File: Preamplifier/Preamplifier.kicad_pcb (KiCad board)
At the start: 2 copper layers, 0 parts

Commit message: Preamplifier Board
Added a preamplifier channel to the board.
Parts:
- added C1: 100n, Capacitor_SMD:C_0805_2012Metric_Pad1.18x1.45mm_HandSolder, F.Cu at (161.0, 84.0)
- added C10: 100n, Capacitor_SMD:C_0805_2012Metric_Pad1.18x1.45mm_HandSolder, F.Cu at (165.3, 144.2)
- added C11: 22n, Capacitor_SMD:C_0805_2012Metric_Pad1.18x1.45mm_HandSolder, F.Cu at (157.5, 94.5)
- added C12: 22n, Capacitor_SMD:C_0805_2012Metric_Pad1.18x1.45mm_HandSolder, F.Cu at (165.3, 147.2)
- added C13: 100n, Capacitor_SMD:C_0805_2012Metric_Pad1.18x1.45mm_HandSolder, F.Cu at (131.9, 137.9)
- added C14: 100n, Capacitor_SMD:C_0805_2012Metric_Pad1.18x1.45mm_HandSolder, F.Cu at (131.9, 140.9)
- added C15: 1u, Capacitor_SMD:C_0805_2012Metric_Pad1.18x1.45mm_HandSolder, F.Cu at (153.5, 91.0)
- added C16: 1u, Capacitor_SMD:C_0805_2012Metric_Pad1.18x1.45mm_HandSolder, F.Cu at (165.3, 150.3)
- added C17: 1u, Capacitor_SMD:C_0805_2012Metric_Pad1.18x1.45mm_HandSolder, F.Cu at (141.0, 88.0)
- added C18: 1u, Capacitor_SMD:C_0805_2012Metric_Pad1.18x1.45mm_HandSolder, F.Cu at (131.9, 143.9)
- added C19: 1u, Capacitor_SMD:C_0805_2012Metric_Pad1.18x1.45mm_HandSolder, F.Cu at (127.5, 85.5)
- added C2: 100n, Capacitor_SMD:C_0805_2012Metric_Pad1.18x1.45mm_HandSolder, F.Cu at (170.0, 84.0)
- added C20: 1u, Capacitor_SMD:C_0805_2012Metric_Pad1.18x1.45mm_HandSolder, F.Cu at (131.9, 146.9)
- added C21: 22u, Capacitor_SMD:CP_Elec_6.3x5.8, F.Cu at (116.5, 83.2)
- added C22: 22u, Capacitor_SMD:CP_Elec_6.3x5.8, F.Cu at (139.6, 140.5)
- added C23: 100n, Capacitor_SMD:C_0805_2012Metric_Pad1.18x1.45mm_HandSolder, F.Cu at (180.7, 79.0)
- added C24: 100n, Capacitor_SMD:C_0805_2012Metric_Pad1.18x1.45mm_HandSolder, F.Cu at (131.9, 149.9)
- added C25: 1u, Capacitor_SMD:C_0805_2012Metric_Pad1.18x1.45mm_HandSolder, F.Cu at (180.7, 83.0)
- added C26: 1u, Capacitor_SMD:C_0805_2012Metric_Pad1.18x1.45mm_HandSolder, F.Cu at (131.9, 153.0)
- added C3: 100p, Capacitor_SMD:C_0805_2012Metric_Pad1.18x1.45mm_HandSolder, F.Cu at (172.5, 91.0)
- added C4: 100p, Capacitor_SMD:C_0805_2012Metric_Pad1.18x1.45mm_HandSolder, F.Cu at (165.3, 138.2)
- added C5: 100n, Capacitor_SMD:C_0805_2012Metric_Pad1.18x1.45mm_HandSolder, F.Cu at (132.5, 92.6)
- added C6: 100n, Capacitor_SMD:C_0805_2012Metric_Pad1.18x1.45mm_HandSolder, F.Cu at (132.5, 83.6)
- added C7: 22u, Capacitor_SMD:CP_Elec_6.3x5.8, F.Cu at (153.5, 83.2)
- added C8: 22u, Capacitor_SMD:CP_Elec_6.3x5.8, F.Cu at (177.7, 140.8)
- added C9: 100n, Capacitor_SMD:C_0805_2012Metric_Pad1.18x1.45mm_HandSolder, F.Cu at (165.3, 141.2)
- added H1: MountingHole, MountingHole:MountingHole_3.2mm_M3, F.Cu at (100.0, 75.0)
- added H2: MountingHole, MountingHole:MountingHole_3.2mm_M3, F.Cu at (192.0, 75.0)
- added H3: MountingHole, MountingHole:MountingHole_3.2mm_M3, F.Cu at (100.0, 125.0)
- added H4: MountingHole, MountingHole:MountingHole_3.2mm_M3, F.Cu at (192.0, 125.0)
- added J1: POWER, Connector_Molex:Molex_KK-254_AE-6410-03A_1x03_P2.54mm_Vertical, F.Cu at (102.0, 102.5)
- added J2: IN_L, Connector_Molex:Molex_KK-254_AE-6410-02A_1x02_P2.54mm_Vertical, F.Cu at (190.0, 93.5)
- added J3: IN_R, Connector_Molex:Molex_KK-254_AE-6410-02A_1x02_P2.54mm_Vertical, F.Cu at (190.0, 104.0)
- added J4: OUT_L, Connector_Molex:Molex_KK-254_AE-6410-02A_1x02_P2.54mm_Vertical, F.Cu at (190.0, 83.5)
- added J5: OUT_R, Connector_Molex:Molex_KK-254_AE-6410-02A_1x02_P2.54mm_Vertical, F.Cu at (190.0, 114.0)
- added R1: 47K, Resistor_SMD:R_0805_2012Metric_Pad1.20x1.40mm_HandSolder, F.Cu at (175.0, 91.0)
- added R10: 10K, Resistor_SMD:R_0805_2012Metric_Pad1.20x1.40mm_HandSolder, F.Cu at (170.1, 150.0)
- added R11: 47K, Resistor_SMD:R_0805_2012Metric_Pad1.20x1.40mm_HandSolder, F.Cu at (141.0, 90.5)
- added R12: 47K, Resistor_SMD:R_0805_2012Metric_Pad1.20x1.40mm_HandSolder, F.Cu at (127.1, 137.9)
- added R13: 90K9, Resistor_SMD:R_0805_2012Metric_Pad1.20x1.40mm_HandSolder, F.Cu at (141.0, 85.5)
- added R14: 90K9, Resistor_SMD:R_0805_2012Metric_Pad1.20x1.40mm_HandSolder, F.Cu at (127.1, 140.8)
- added R15: 6K36, Resistor_SMD:R_0805_2012Metric_Pad1.20x1.40mm_HandSolder, F.Cu at (125.0, 85.5)
- added R16: 6K36, Resistor_SMD:R_0805_2012Metric_Pad1.20x1.40mm_HandSolder, F.Cu at (127.1, 143.8)
- added R17: 2K7, Resistor_SMD:R_0805_2012Metric_Pad1.20x1.40mm_HandSolder, F.Cu at (125.0, 89.5)
- added R18: 2K7, Resistor_SMD:R_0805_2012Metric_Pad1.20x1.40mm_HandSolder, F.Cu at (127.1, 146.7)
- added R19: 100K, Resistor_SMD:R_0805_2012Metric_Pad1.20x1.40mm_HandSolder, F.Cu at (127.5, 89.5)
- added R2: 47K, Resistor_SMD:R_0805_2012Metric_Pad1.20x1.40mm_HandSolder, F.Cu at (170.1, 138.2)
- added R20: 100K, Resistor_SMD:R_0805_2012Metric_Pad1.20x1.40mm_HandSolder, F.Cu at (127.1, 149.7)
- added R21: 750, Resistor_SMD:R_0805_2012Metric_Pad1.20x1.40mm_HandSolder, F.Cu at (178.2, 78.9)
- added R22: 750, Resistor_SMD:R_0805_2012Metric_Pad1.20x1.40mm_HandSolder, F.Cu at (127.1, 152.6)
- added R23: 100K, Resistor_SMD:R_0805_2012Metric_Pad1.20x1.40mm_HandSolder, F.Cu at (178.2, 83.0)
- added R24: 100K, Resistor_SMD:R_0805_2012Metric_Pad1.20x1.40mm_HandSolder, F.Cu at (127.1, 155.6)
- added R3: 2K2, Resistor_SMD:R_0805_2012Metric_Pad1.20x1.40mm_HandSolder, F.Cu at (170.0, 91.0)
- added R4: 2K2, Resistor_SMD:R_0805_2012Metric_Pad1.20x1.40mm_HandSolder, F.Cu at (170.1, 141.1)
- added R5: 4K7, Resistor_SMD:R_0805_2012Metric_Pad1.20x1.40mm_HandSolder, F.Cu at (161.0, 91.0)
- added R6: 4K7, Resistor_SMD:R_0805_2012Metric_Pad1.20x1.40mm_HandSolder, F.Cu at (170.1, 144.1)
- added R7: 180K, Resistor_SMD:R_0805_2012Metric_Pad1.20x1.40mm_HandSolder, F.Cu at (158.5, 91.0)
- added R8: 180K, Resistor_SMD:R_0805_2012Metric_Pad1.20x1.40mm_HandSolder, F.Cu at (170.1, 147.0)
- added R9: 10K, Resistor_SMD:R_0805_2012Metric_Pad1.20x1.40mm_HandSolder, F.Cu at (156.0, 91.0)
- added U1: OPA1612AxD, Package_SO:SOIC-8_3.9x4.9mm_P1.27mm, F.Cu at (165.5, 85.5)
- added U2: OPA1612AxD, Package_SO:SOIC-8_3.9x4.9mm_P1.27mm, F.Cu at (134.0, 88.0)
- added U3: OPA1612AxD, Package_SO:SOIC-8_3.9x4.9mm_P1.27mm, F.Cu at (176.7, 148.2)
- added U4: OPA1612AxD, Package_SO:SOIC-8_3.9x4.9mm_P1.27mm, F.Cu at (138.6, 147.9)
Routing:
- net Net-(R19-Pad2): track 0.00 -> 105.4 mm
- net -12V: track 0.00 -> 76.4 mm, vias 0 -> 2
- net +12V: track 0.00 -> 68.2 mm, vias 0 -> 2
- net Net-(J2-Pin_2): track 0.00 -> 23.3 mm
- net Net-(U2A--): track 0.00 -> 16.6 mm
- net Net-(C15-Pad2): track 0.00 -> 14.7 mm
- net Net-(J4-Pin_2): track 0.00 -> 12.6 mm
- net Net-(U1A--): track 0.00 -> 11.3 mm
- net Net-(C21-Pad1): track 0.00 -> 10.2 mm
- net Net-(C7-Pad1): track 0.00 -> 9.20 mm
- net Net-(U2B--): track 0.00 -> 7.82 mm
- net Net-(U2B-+): track 0.00 -> 6.92 mm
- net Net-(U2A-+): track 0.00 -> 6.26 mm
- net Net-(U1A-+): track 0.00 -> 5.50 mm
- net Net-(C15-Pad1): track 0.00 -> 5.02 mm
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- added copper zone on B.Cu, net GND
- added copper zone on F.Cu, net GND
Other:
- board outline added: 100 x 58 mm

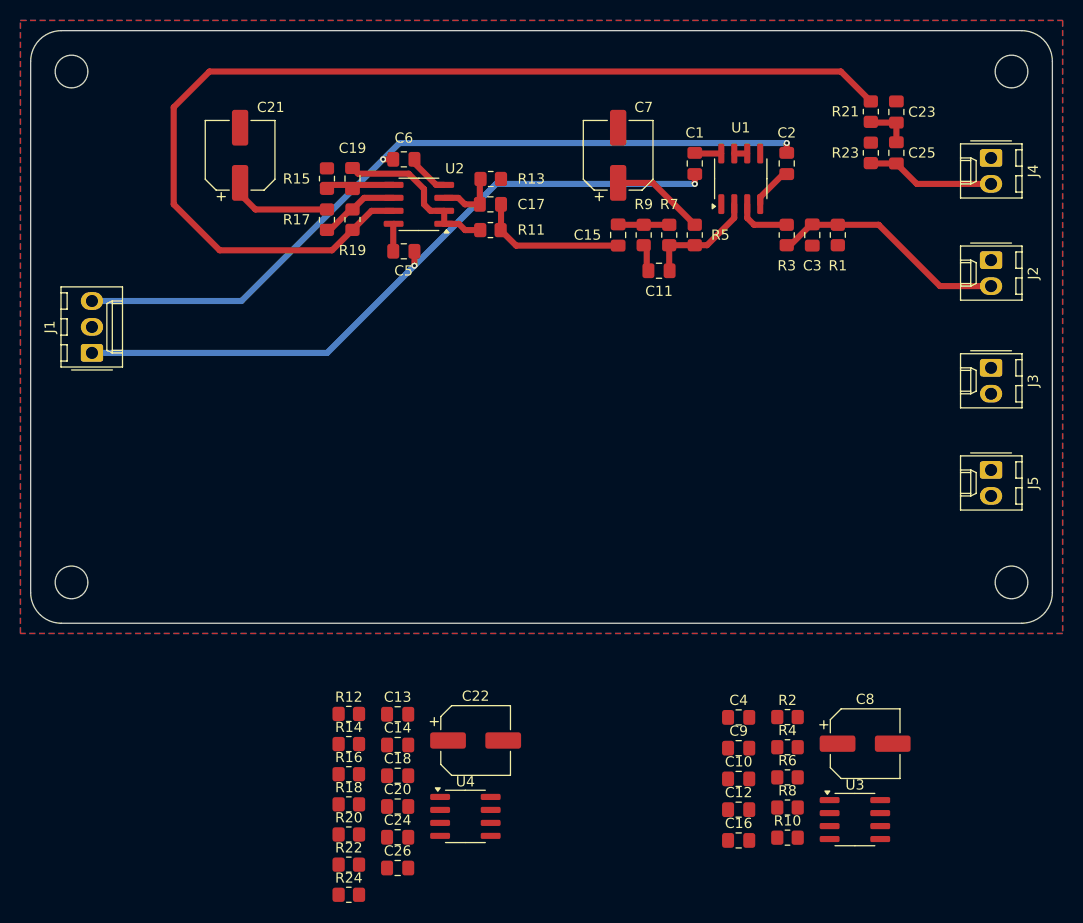
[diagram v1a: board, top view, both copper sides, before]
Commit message: Preamplifier Board
Updated the preamplifier board design.
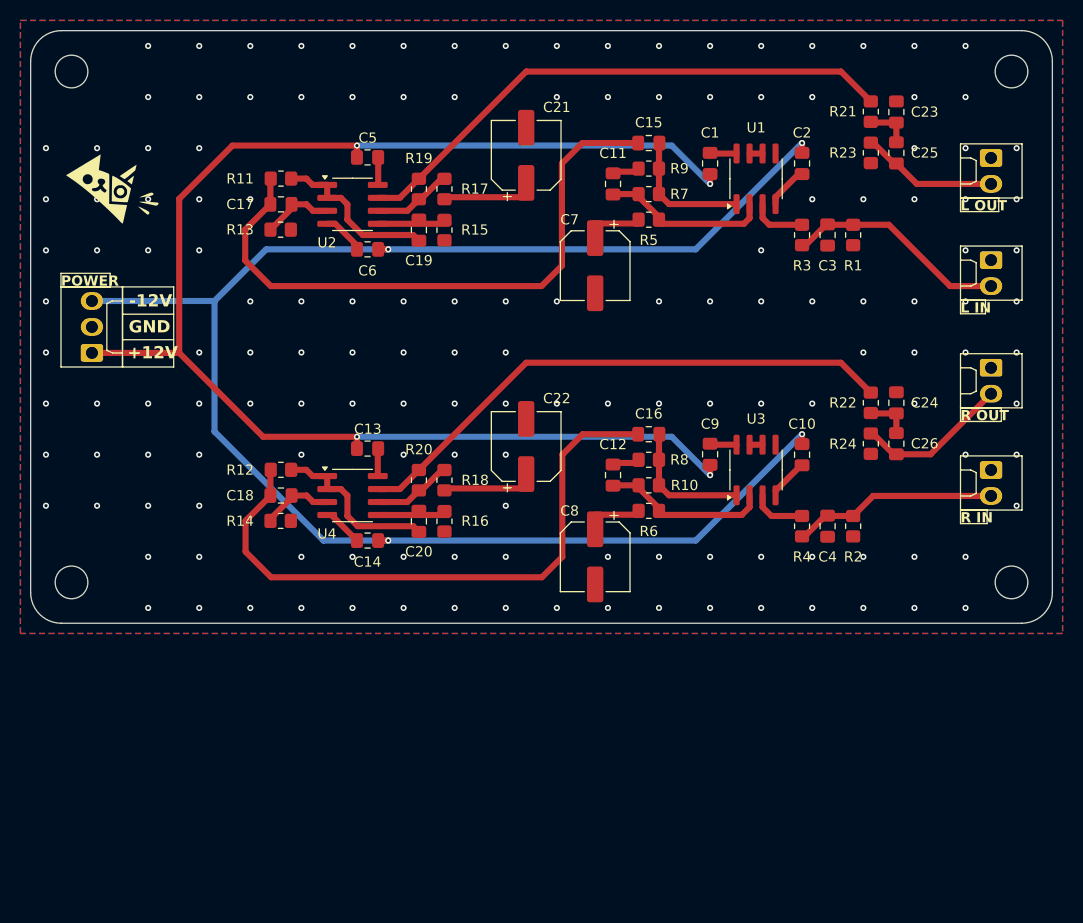
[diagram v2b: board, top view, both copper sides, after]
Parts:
- added G***: LOGO, Logos:Cat, F.Cu at (104.0, 86.5)
- J1: footprint Connector_Molex:Molex_KK-254_AE-6410-03A_1x03_P2.54mm_Vertical -> Custom_Parts:Molex_KK-254_1x03_P2.54mm_Vertical
- J2, J3, J4, J5: footprint Connector_Molex:Molex_KK-254_AE-6410-02A_1x02_P2.54mm_Vertical -> Custom_Parts:Molex_KK-254_1x02_P2.54mm_Vertical
- moved R22 68.2 mm to (178.2, 107.4), turned to -90 degrees
- moved R24 67.5 mm to (178.2, 111.4), turned to -90 degrees
- moved C24 64.7 mm to (180.7, 107.4), turned to 90 degrees
- moved C26 64.1 mm to (180.7, 111.4), turned to 90 degrees
- moved C16 40.7 mm to (156.5, 110.5), turned to 180 degrees
- moved R8 39.4 mm to (156.5, 113.0)
- moved U3 35.6 mm to (167.0, 114.0), turned to 90 degrees
- moved R20 35.3 mm to (134.0, 115.0), turned to 90 degrees
- moved C12 35.0 mm to (153.0, 114.5), turned to 90 degrees
- moved R10 34.3 mm to (156.5, 115.5)
- moved U4 33.3 mm to (127.5, 116.5)
- moved R18 33.1 mm to (136.5, 115.0), turned to -90 degrees
- moved C10 32.3 mm to (171.5, 112.5), turned to 90 degrees
- moved C8 32.1 mm to (151.2, 122.5), turned to -90 degrees
- moved C18 29.7 mm to (120.5, 116.5)
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- renumbered R8 to R10, R10 to R8
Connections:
- C26 pad 1: Net-(C24-Pad1) -> Net-(J5-Pin_2)
- C26 pad 2: Net-(J5-Pin_2) -> Net-(C24-Pad1)
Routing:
- net -12V: track 76.4 -> 158.8 mm, vias 2 -> 4
- net +12V: track 68.2 -> 140.5 mm, vias 2 -> 4
- net Net-(C16-Pad2): track 0.00 -> 60.2 mm
- net Net-(R20-Pad2): track 0.00 -> 54.6 mm
- net Net-(R19-Pad2): track 105.4 -> 54.6 mm
- net Net-(C15-Pad2): track 14.7 -> 60.2 mm
- net Net-(J3-Pin_2): track 0.00 -> 19.7 mm
- net Net-(U4A--): track 0.00 -> 16.9 mm
- net Net-(U3A--): track 0.00 -> 15.7 mm
- net Net-(J5-Pin_2): track 0.00 -> 14.6 mm
- net Net-(C16-Pad1): track 0.00 -> 13.0 mm
- net Net-(C22-Pad1): track 0.00 -> 8.00 mm
- net Net-(C15-Pad1): track 5.02 -> 13.0 mm
- net Net-(U4B--): track 0.00 -> 7.32 mm
- net Net-(U4B-+): track 0.00 -> 6.70 mm
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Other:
- board text added: "+12V"
- board text added: "-12V"
- board text added: "GND"
- board text added: "L IN"
- board text added: "L OUT"
- board text added: "PD 08/25"
- board text added: "PHONO PREAMP"
- board text added: "POWER"
- board text added: "R IN"
- board text added: "R OUT"
- board text added: "REV A"
- board text added: "VERSION 1.0"

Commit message: Board Designs
Updated the power supply board design.
Updated the preamplifier board design.
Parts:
- added G***: LOGO, Logos:PhonoPreamp, B.Cu at (146.3, 100.0)
